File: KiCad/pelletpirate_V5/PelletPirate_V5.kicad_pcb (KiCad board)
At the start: 2 copper layers, 65 x 110 mm, 136 parts, among them J1 SJ1-3523NG_Jack_PP, J2 SJ1-3523NG_Jack_PP, J3 SJ1-3523NG_Jack_PP, J4 SJ1-3523NG_Jack_PP, J5 SJ1-3523NG_Jack_PP, J6 Conn_01x04, J7 Conn_01x04_Socket, J8 USB4145-03-0170-C, J9 TB002-500-02BE, T1 BTA12-600BWRG, T2 BTA12-600BWRG, T3 BTA12-600BWRG, U1 USBLC6-2SC6, U3 H11AA1M

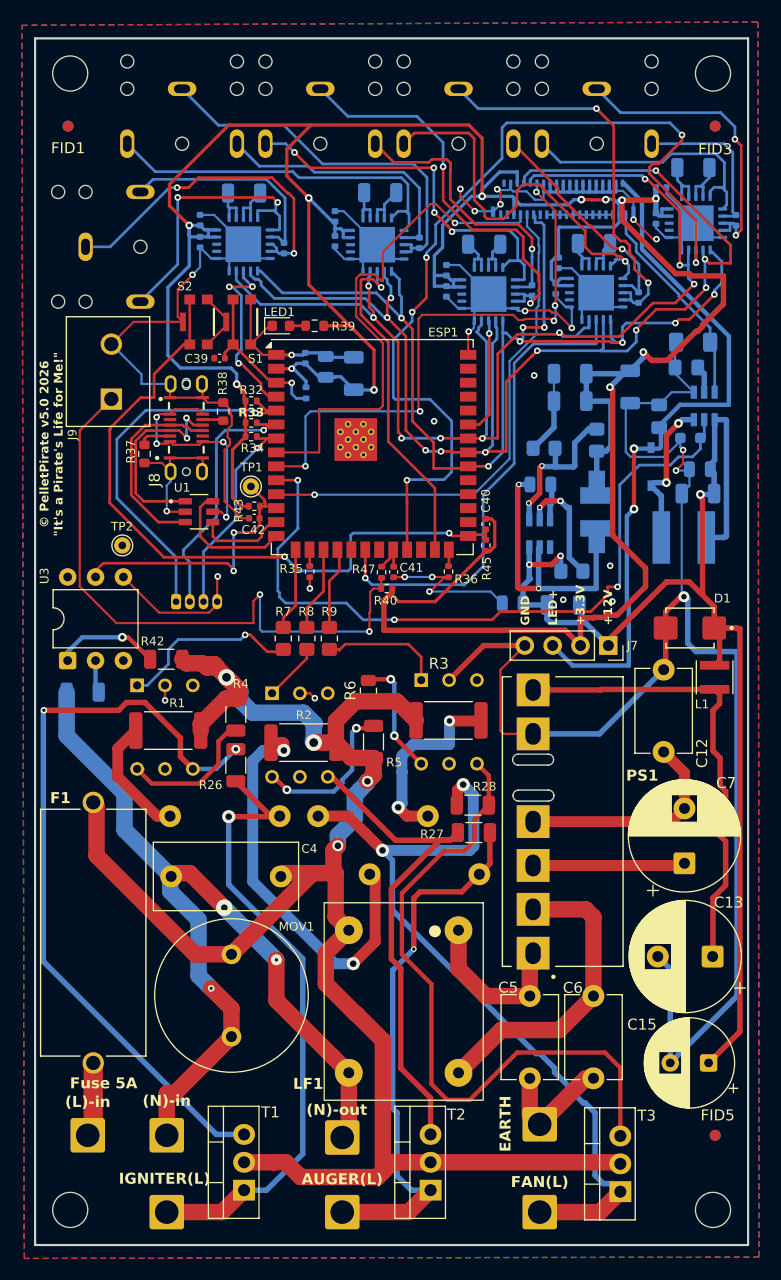
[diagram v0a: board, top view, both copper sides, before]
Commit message: V5 post-cancel fixes: C9 0402, C43 VBUS ballast, C39/C40 boot pair, R20 0805
Order cancelled 2026-08-28; V5 is the active design again. Fixes since:
- C9: footprint corrected to 0402, MPN C0402C104K3RACTU (package now matches part)
- C43 NEW: 100nF 0402 at U1 pin 5, /VBUS->GND ESD ballast (verified 1.63mm from pin)
- C39: EN cap 0.1uF -> 1.0uF 25V KEMET C0603C105K3RACTU (0603 X7R) per Espressif
- C40: IO0 debounce cap rewired +3.3V -> GND (orthodox; linked with C39 change,
  EN delay 10ms >> IO0 rise 1ms, boot-strap race eliminated)
- R20: MPN corrected to RC0805FR-0710KL, footprint normalized to plain 0805
Audits passed on this state: ESP32 pin-by-pin (zero notes), MAX1-5 tiles,
H11AA1/MOC3053, J8/U1 USB, full board-symbol-footprint-BOM reconciliation
(118 refs, 70 package-decoded lines, 0 errors). ERC 0 / DRC 0 / parity 0.

Co-Authored-By: Claude Fable 5 <noreply@anthropic.com>
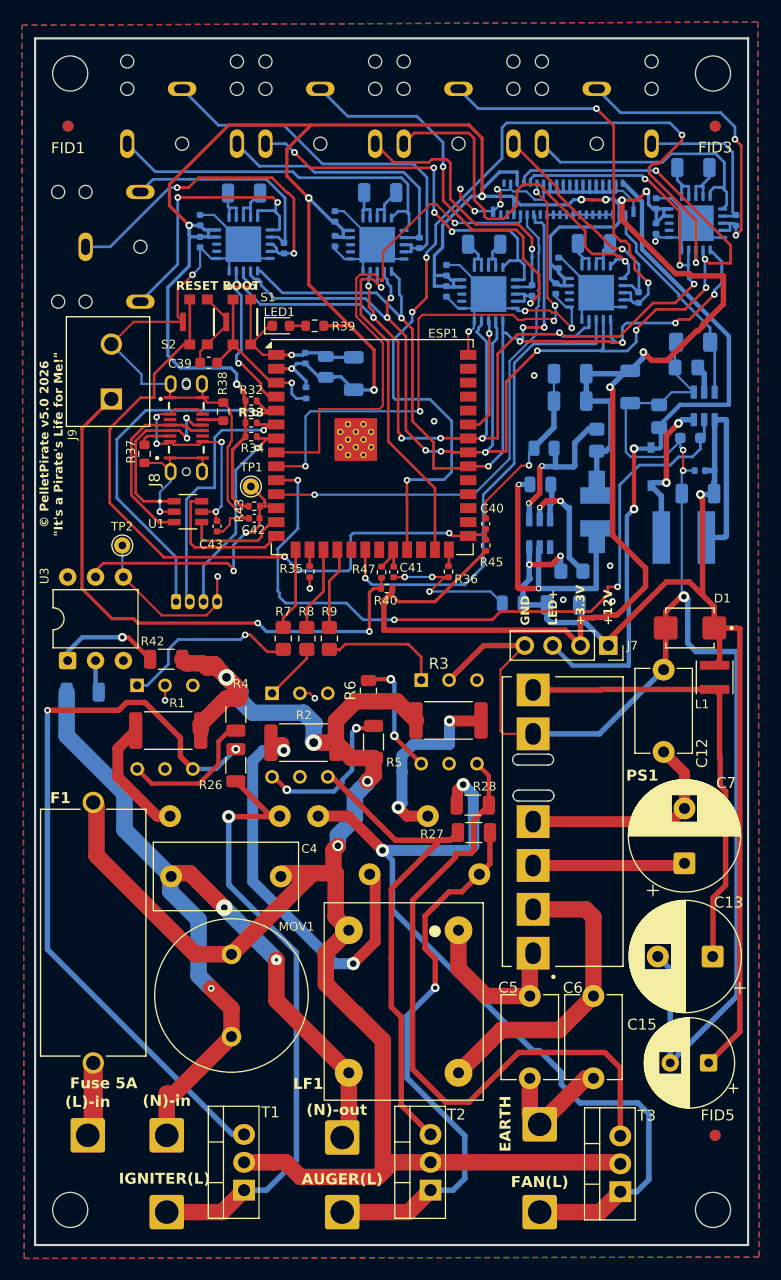
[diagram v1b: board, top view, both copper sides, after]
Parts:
- added C43: 0.1µF 25V, Capacitor_SMD:C_0402_1005Metric, F.Cu at (136.6, 84.5)
- C39: value 0.1µF 25V -> 1.0µF 25V; footprint Capacitor_SMD:C_0402_1005Metric -> Capacitor_SMD:C_0603_1608Metric
- C9: footprint Capacitor_SMD:C_0805_2012Metric -> Capacitor_SMD:C_0402_1005Metric
- R20: footprint Resistor_SMD:R_0805_2012Metric_Pad1.20x1.40mm_HandSolder -> Resistor_SMD:R_0805_2012Metric
- moved C35 1.52 mm to (176.6, 55.1), turned to -90 degrees
- moved C39 1.08 mm to (135.8, 69.6)
- moved U1 1.01 mm to (133.9, 83.2)
- moved C25 0.92 mm to (176.6, 57.3)
- moved C9 0.12 mm to (180.6, 79.4)
- turned C34 to -90 degrees
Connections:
- C40 pad 2: +3.3V -> GND
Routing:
- net GND: track 380.3 -> 393.9 mm
- net Net-(T3-A1): track 72.8 -> 78.5 mm
- net Net-(J9-Pad1): track 57.3 -> 52.0 mm
- net /USB_D+: track 11.8 -> 13.2 mm
- net Net-(T1-G): track 69.9 -> 68.5 mm
- net +3.3V: track 309.2 -> 307.9 mm
- net /USB_D-: track 8.21 -> 9.38 mm
- net Net-(PS1-+VO): track 43.8 -> 42.7 mm
- net /USB-C_D+: track 18.6 -> 17.6 mm
- net /USB-C_D-: track 18.3 -> 17.3 mm
- net Net-(T2-A1): track 49.8 -> 50.7 mm
- net /Encoder_OutB: track 24.2 -> 25.0 mm
- net Net-(ESP1-EN): track 14.9 -> 15.6 mm
- net Net-(T3-G): track 61.5 -> 60.9 mm
- net /ZC_DET: track 25.7 -> 25.0 mm
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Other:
- board text added: "BOOT"
- board text added: "RESET"

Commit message: V5 raft complete: 4 work packages + C48 damping bulk, all audited, ERC/DRC/netclass clean
WP1: C44/C45 22uF at ESP (raft bulk). WP2: 33R series R at SPI driver pads (R48-51,
stubs <2.2mm). WP3: FL1 bead + C46/C47 panel island (/3V3_LCD, FPC-only membership).
WP4: L5 HF bead after Fig-2 network (D1/C15 upstream preserved) + C48 220uF damping
bulk (resonance 50k->12kHz, Q~1). Netclass patterns added for /3V3_LCD + Net-(C15-Pad1).
EE-soundness review: resonances quantified, Middlebrook margin 80x, timing budgets clear.
Acceptance: runt sentinel 0/min on AC at first article.

Co-Authored-By: Claude Fable 5 <noreply@anthropic.com>
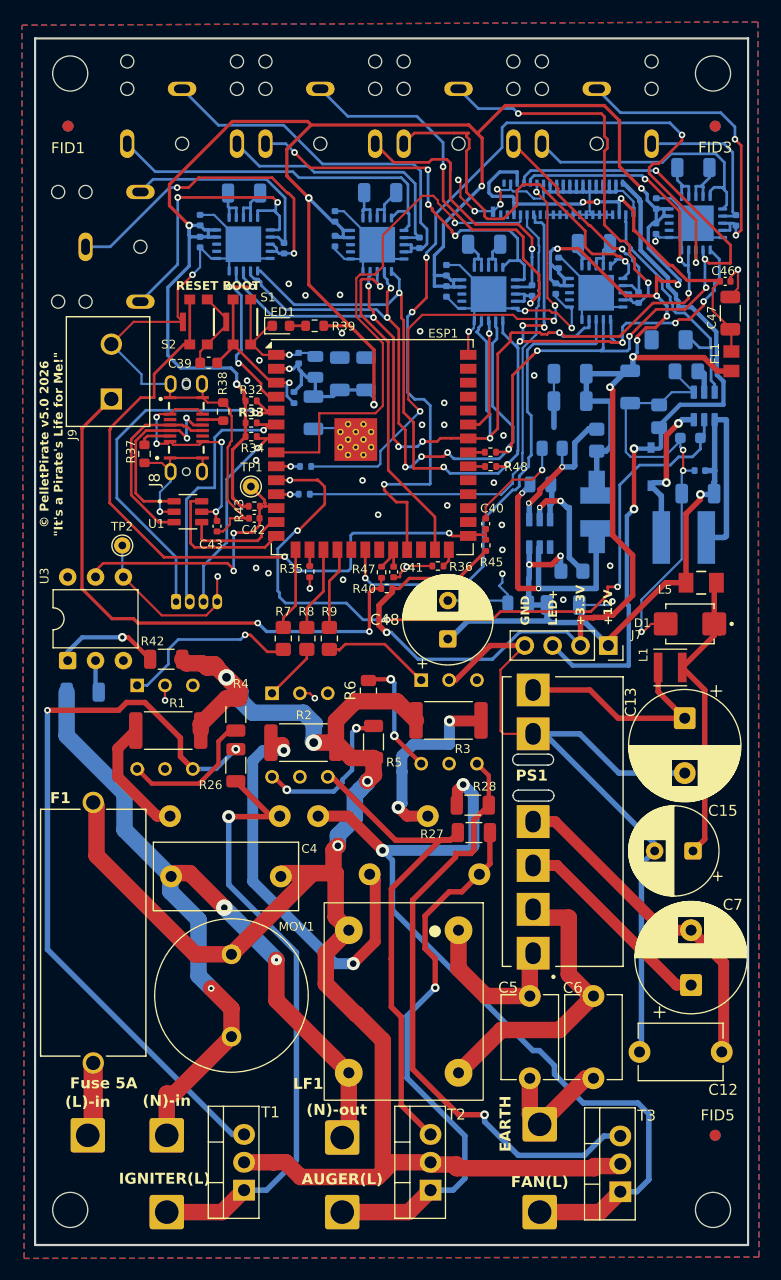
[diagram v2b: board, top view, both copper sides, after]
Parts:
- added C44: 22µF 16V, Capacitor_SMD:C_1206_3216Metric, B.Cu at (147.8, 70.6)
- added C45: 22µF 16V, Capacitor_SMD:C_1206_3216Metric, B.Cu at (150.2, 70.6)
- added C46: 0.1µF 16V, Capacitor_SMD:C_0402_1005Metric, F.Cu at (182.9, 62.1)
- added C47: 22µF 16V, Capacitor_SMD:C_1206_3216Metric, F.Cu at (183.4, 65.0)
- added C48: 220µF 35V, Capacitor_THT:CP_Radial_D8.0mm_P3.50mm, F.Cu at (157.6, 94.8)
- added FL1: BLM21PG221SN1D, Ferrite_Bead:BEADC2012X105N, F.Cu at (183.5, 69.4)
- added L5: IND_BLM31PG391SN1L_MUR, Ferrite_Bead_12V:IND_BLM31PG391SN1L_MUR, F.Cu at (180.7, 89.6)
- added R48: 33Ω, Resistor_SMD:R_0402_1005Metric, F.Cu at (161.5, 79.0)
- added R49: 33Ω, Resistor_SMD:R_0402_1005Metric, F.Cu at (161.5, 77.7)
- added R50: 33Ω, Resistor_SMD:R_0402_1005Metric, B.Cu at (144.7, 79.0)
- added R51: 33Ω, Resistor_SMD:R_0402_1005Metric, B.Cu at (144.5, 81.5)
- moved C12 27.9 mm to (182.6, 132.4), turned to 180 degrees
- moved C13 21.9 mm to (179.2, 102.0), turned to -90 degrees
- moved C15 19.4 mm to (180.0, 114.1)
- moved C7 11.1 mm to (179.8, 126.3)
- moved C38 5.13 mm to (145.4, 74.1), turned to -90 degrees
- moved L1 4.15 mm to (177.9, 97.3), turned to 0 degrees
- moved R17 2.25 mm to (177.8, 67.5)
- moved R44 1.18 mm to (143.6, 72.7)
- moved R36 1.09 mm to (156.7, 88.1), turned to 180 degrees
- moved C37 0.95 mm to (145.6, 70.0)
- moved R20 0.74 mm to (167.1, 77.4)
- moved C17 0.61 mm to (144.0, 69.2)
- moved C11 0.51 mm to (164.1, 91.5)
- moved D1 0.38 mm to (179.7, 93.4)
- moved C36 0.35 mm to (179.4, 70.3)
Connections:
- C15 pad 1: +12V -> Net-(C15-Pad1)
- D1 pad 1: +12V -> Net-(C15-Pad1)
- ESP1 pad 11: /LCD_DC -> Net-(ESP1-IO18)
- ESP1 pad 32: /ALL_SDI -> Net-(ESP1-IO39)
- ESP1 pad 33: /ALL_SCLK -> Net-(ESP1-IO40)
- ESP1 pad 9: /LCD_CS -> Net-(ESP1-IO16)
- FPC1 pad 3: +3.3V -> /3V3_LCD
- FPC1 pad 34: +3.3V -> /3V3_LCD
- FPC1 pad 35: +3.3V -> /3V3_LCD
- L1 pad 2: +12V -> Net-(C15-Pad1)
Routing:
- net +12V: track 114.9 -> 71.3 mm
- net /3V3_LCD: track 0.00 -> 41.0 mm, vias 0 -> 3
- net Net-(C15-Pad1): track 0.00 -> 28.0 mm
- net Net-(PS1-+VO): track 42.7 -> 20.5 mm
- net GND: track 393.9 -> 376.2 mm, vias 27 -> 47
- net Net-(PS1--V(CAP)): track 20.5 -> 31.5 mm
- net +3.3V: track 307.9 -> 316.1 mm, vias 12 -> 15
- net Net-(T3-G): track 60.9 -> 55.3 mm, vias 0 -> 1
- net /ALL_SCLK: track 114.9 -> 120.2 mm, vias 10 -> 11
- net Net-(PS1-+V(CAP)): track 13.9 -> 18.9 mm
- net /LCD_CS: track 52.5 -> 48.1 mm, vias 5 -> 4
- net /ALL_SDI: track 97.7 -> 101.1 mm, vias 8 -> 9
- net /LED_PWM: track 67.7 -> 71.0 mm, vias 3 -> 4
- net /LED-: track 19.6 -> 22.6 mm
- net Net-(ESP1-IO16): track 0.00 -> 2.17 mm, vias 0 -> 1
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
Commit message: V5 PCBWay package regenerated: raft revision, 61 lines / 129 components, 19 no-sub lines
Gerbers+drill (25 slots), positions (148), BOM with FL1/L5/C13/C15+C48 no-sub additions,
assembly notes updated (J9 orientation, C48 polarity, supersedes cancelled 08-27 upload).
Old package archived to archive_to_delete/. L5 601 value+footprint+3D model settled.
J9 flipped: entry faces west edge. Final ERC/DRC 0/0, parity 142/142.

Co-Authored-By: Claude Fable 5 <noreply@anthropic.com>
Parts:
- L5: value IND_BLM31PG391SN1L_MUR -> BLM31PG601SN1L; footprint Ferrite_Bead_12V:IND_BLM31PG391SN1L_MUR -> Ferrite_Bead_12V_Flyman:BEADC3216X130N_flyman
- moved J9 4.80 mm to (127.0, 68.1), turned to -90 degrees
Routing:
- net Net-(J9-Pad1): track 52.0 -> 56.8 mm
- net GND: track 376.2 -> 377.4 mm
